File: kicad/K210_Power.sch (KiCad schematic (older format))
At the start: 18 parts, among them U1 K210, Y1 26MHz

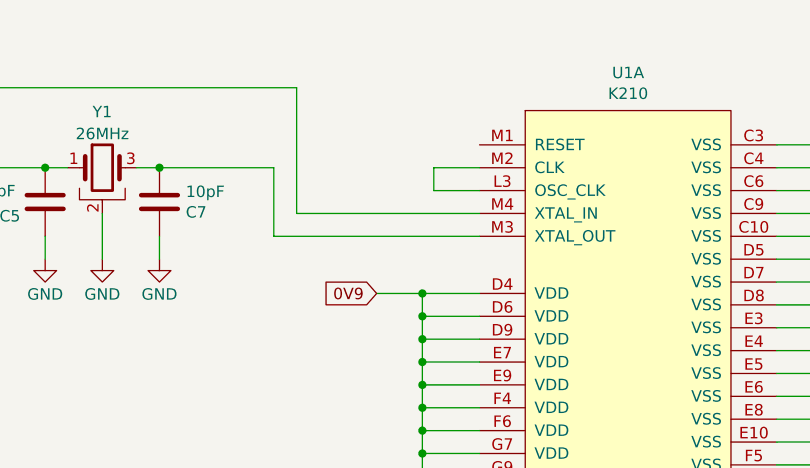
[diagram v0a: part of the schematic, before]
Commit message: ESP32 added to schematic. ESP32 refs. Slight mod to block diagram.
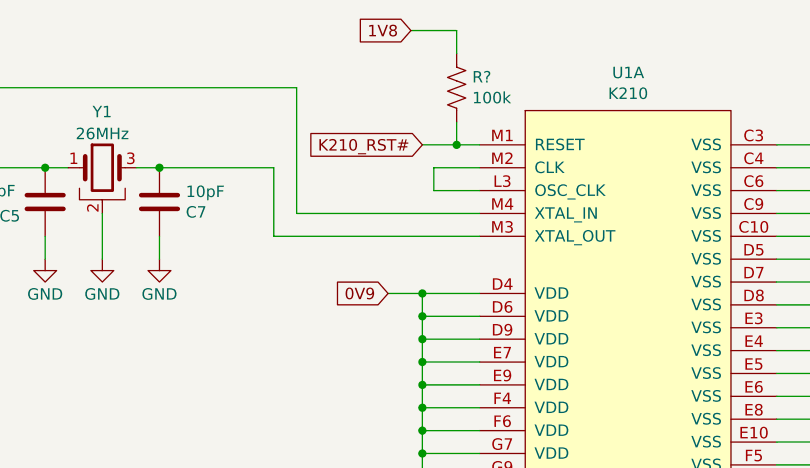
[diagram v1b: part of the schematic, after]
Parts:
- added R?: 100k, symbol Device:R_US
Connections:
- net 1V8: now also R?.1
- net K210_RST#: now reaches U1.M1 (RESET)
- net K210_RST#: now also R?.2
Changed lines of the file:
@@
 $Descr A4 11693 8268
 encoding utf-8
-Sheet 3 3
+Sheet 3 4
 Title ""
 Date ""
@@
 	4550 5700 4800 5700
 Wire Wire Line
-	4600 2350 4800 2350
+	4650 2350 4800 2350
 Wire Wire Line
 	4650 3850 4800 3850
@@
 Text GLabel 4050 5300 0    50   Input ~ 0
 0V9
-Text GLabel 4600 2350 0    50   Input ~ 0
+Text GLabel 4650 2350 0    50   Input ~ 0
 0V9
 Text GLabel 4650 3850 0    50   Input ~ 0
@@
 	1    0    0    -1
 $EndComp
+Text GLabel 4800 1700 0    50   Input ~ 0
+K210_RST#
+Wire Wire Line
+	4800 1700 4950 1700
+Text GLabel 4750 1200 0    50   Input ~ 0
+1V8
+$Comp
+L Device:R_US R?
+U 1 1 5EB28978
+P 4950 1450
+F 0 "R?" H 5018 1496 50  0000 L CNN
+F 1 "100k" H 5018 1405 50  0000 L CNN
+F 2 "" V 4990 1440 50  0001 C CNN
+F 3 "~" H 4950 1450 50  0001 C CNN
+	1    4950 1450
+	1    0    0    -1
+$EndComp
+Wire Wire Line
+	4950 1300 4950 1200
+Wire Wire Line
+	4950 1200 4750 1200
+Wire Wire Line
+	4950 1600 4950 1700
+Connection ~ 4950 1700
+Wire Wire Line
+	4950 1700 5050 1700
 $EndSCHEMATC
